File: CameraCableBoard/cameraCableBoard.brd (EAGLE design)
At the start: 22.8 x 17.4 mm, 2 parts, among them J2 FLEXCABLE-SFW15R-1STE1LF

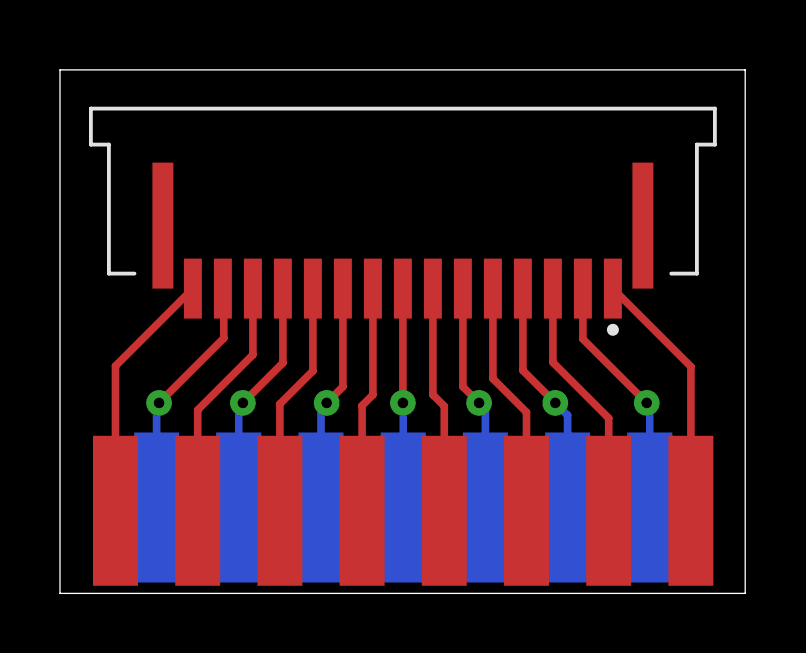
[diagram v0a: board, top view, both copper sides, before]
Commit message: New 3x3 panelized camera converter boards
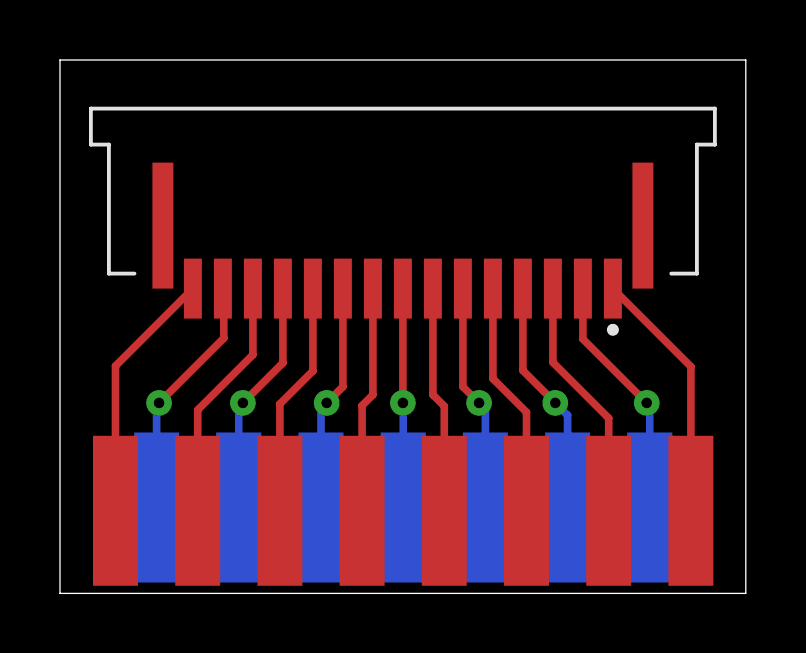
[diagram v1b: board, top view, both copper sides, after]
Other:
- board size 22.8 x 17.4 mm -> 22.9 x 17.8 mm
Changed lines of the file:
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@@
 <layer number="43" name="vRestrict" color="2" fill="10" visible="yes" active="yes"/>
 <layer number="44" name="Drills" color="7" fill="1" visible="no" active="yes"/>
-<layer number="45" name="Holes" color="7" fill="1" visible="no" active="yes"/>
+<layer number="45" name="Holes" color="7" fill="1" visible="yes" active="yes"/>
 <layer number="46" name="Milling" color="3" fill="1" visible="no" active="yes"/>
 <layer number="47" name="Measures" color="7" fill="1" visible="no" active="yes"/>
@@
 <board>
 <plain>
-<wire x1="0" y1="0" x2="22.84" y2="0" width="0" layer="20"/>
-<wire x1="22.84" y1="0" x2="22.84" y2="17.45" width="0" layer="20"/>
-<wire x1="22.84" y1="17.45" x2="0" y2="17.45" width="0" layer="20"/>
-<wire x1="0" y1="17.45" x2="0" y2="0" width="0" layer="20"/>
+<wire x1="0" y1="0" x2="22.86" y2="0" width="0" layer="20"/>
+<wire x1="22.86" y1="0" x2="22.86" y2="17.78" width="0" layer="20"/>
+<wire x1="22.86" y1="17.78" x2="0" y2="17.78" width="0" layer="20"/>
+<wire x1="0" y1="17.78" x2="0" y2="0" width="0" layer="20"/>
 <text x="23.876" y="7.366" size="1.27" layer="51">Estimated Clock Skew: 3.8picoseconds</text>
 </plain>
